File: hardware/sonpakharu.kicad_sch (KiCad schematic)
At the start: 48 parts, among them IC1 ESP32-S3-WROOM-1U-N4, J1 FTDI, J10 EXT4, J11 EXT5, J12 EXT6, J13 EXT7, J14 EXT8, J15 BATT, J16 PWR, J2 ADC1, J3 ADC2, J4 ADC3, J5 ADC4, J6 I2C, J7 EXT1, J8 EXT2, J9 EXT3, Q1 DMG2301L, Q2 S8050, Q3 S8050, SW1 Reset, SW2 Reset, U1 AP2112K-3.3TRG1, U2 MCP73831-2-OT, U3 ADS1115IDGSR

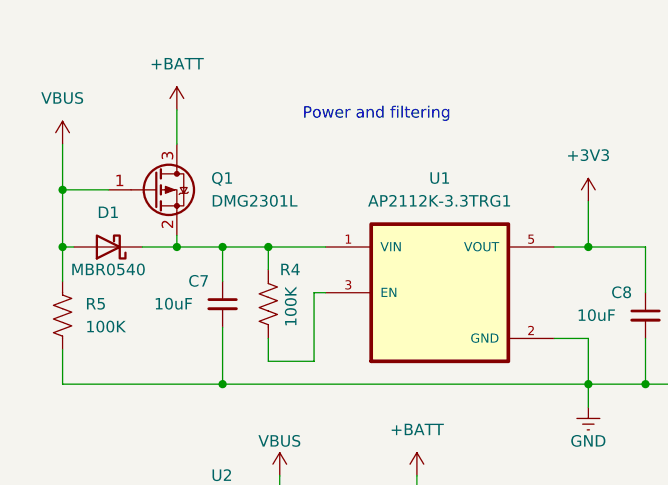
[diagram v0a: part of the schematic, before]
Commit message: added main components mpn
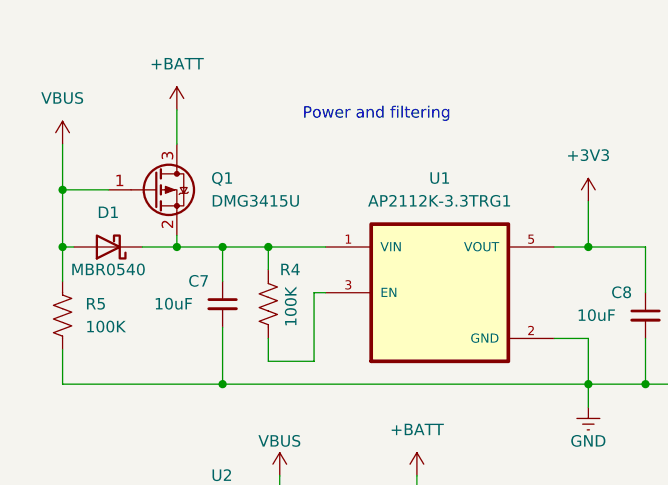
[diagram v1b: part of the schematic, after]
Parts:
- Q1: value DMG2301L -> DMG3415U; MPN (none) -> C96616
- U1: MPN (none) -> C51118
- U2: MPN (none) -> C424093
- U3: MPN (none) -> C37593
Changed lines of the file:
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@@
+      (effects (font (size 1.27 1.27)) hide)
+    )
+    (property "MPN" "C424093" (at 43.18 80.01 0)
       (effects (font (size 1.27 1.27)) hide)
     )
@@
       (effects (font (size 1.27 1.27)) (justify bottom) hide)
     )
+    (property "MPN" "C51118" (at 60.96 48.26 0)
+      (effects (font (size 1.27 1.27)) hide)
+    )
     (pin "1")
     (pin "2")
@@
       (effects (font (size 1.27 1.27)) (justify left))
     )
-    (property "Value" "DMG2301L" (at 35.56 38.1 0)
+    (property "Value" "DMG3415U" (at 35.56 38.1 0)
       (effects (font (size 1.27 1.27)) (justify left))
     )
@@
       (effects (font (size 1.27 1.27)) (justify left) hide)
     )
+    (property "MPN" "C96616" (at 29.21 36.83 0)
+      (effects (font (size 1.27 1.27)) hide)
+    )
     (pin "1")
     (pin "2")
@@
       (effects (font (size 1.27 1.27)) (justify bottom) hide)
     )
-    (pin "1")
+    (property "MPN" "C37593" (at 137.16 172.72 0)
+      (effects (font (size 1.27 1.27)) hide)
+    )
+    (pin "1")

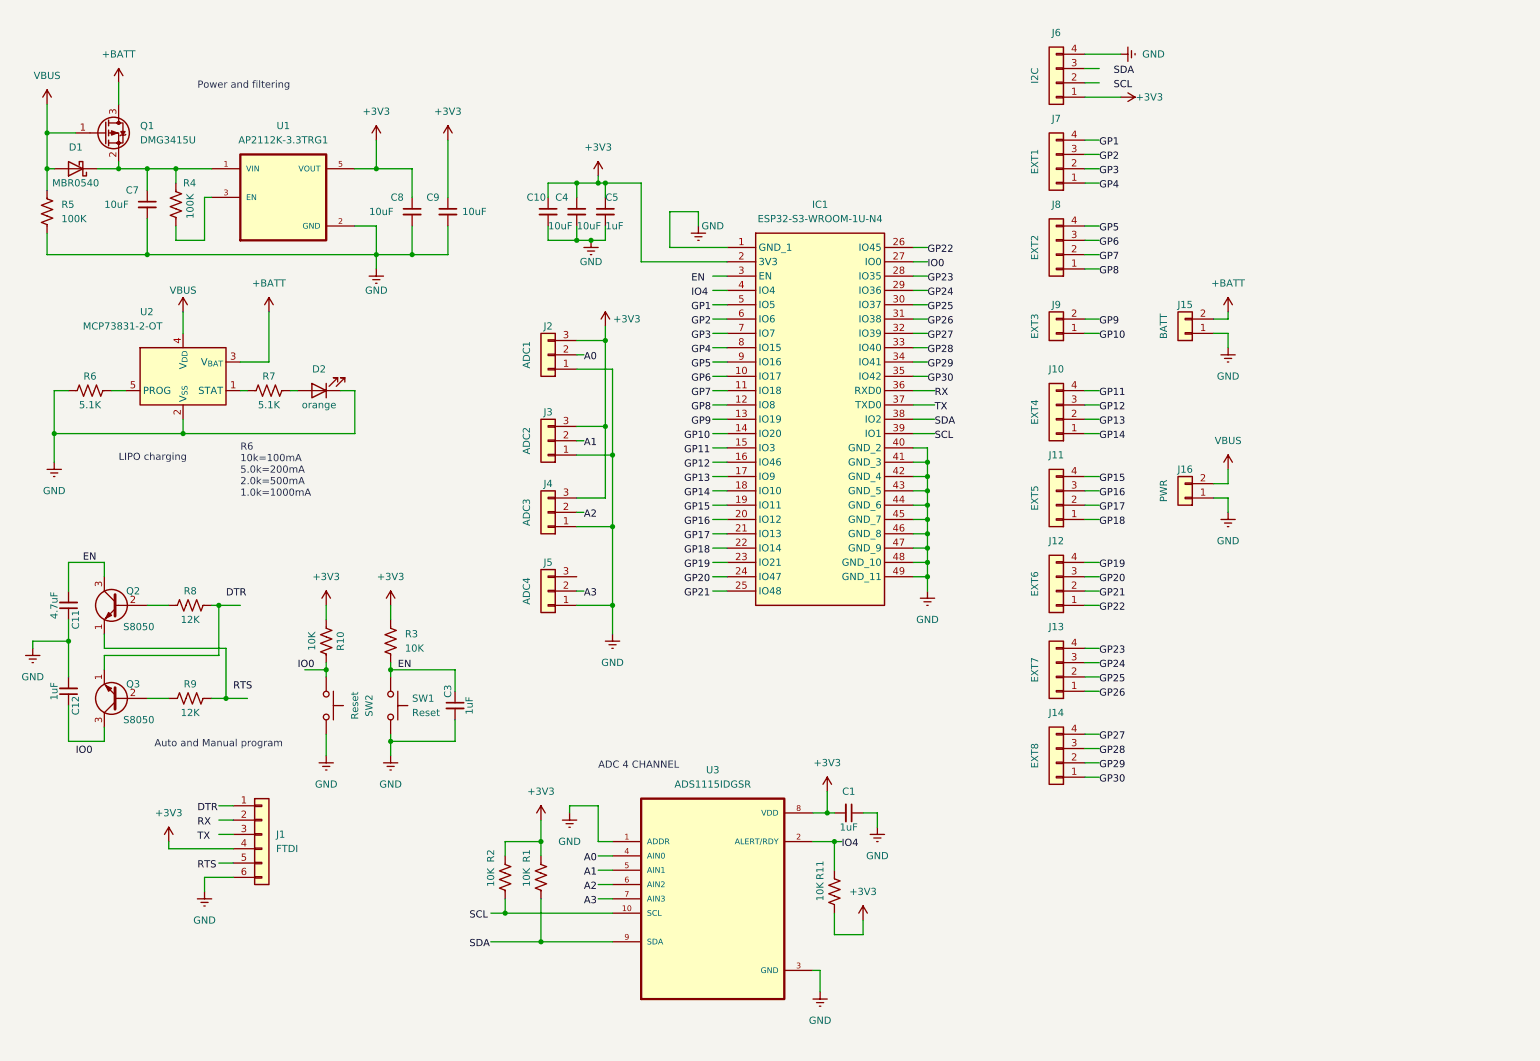
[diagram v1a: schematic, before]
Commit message: Fix: routing
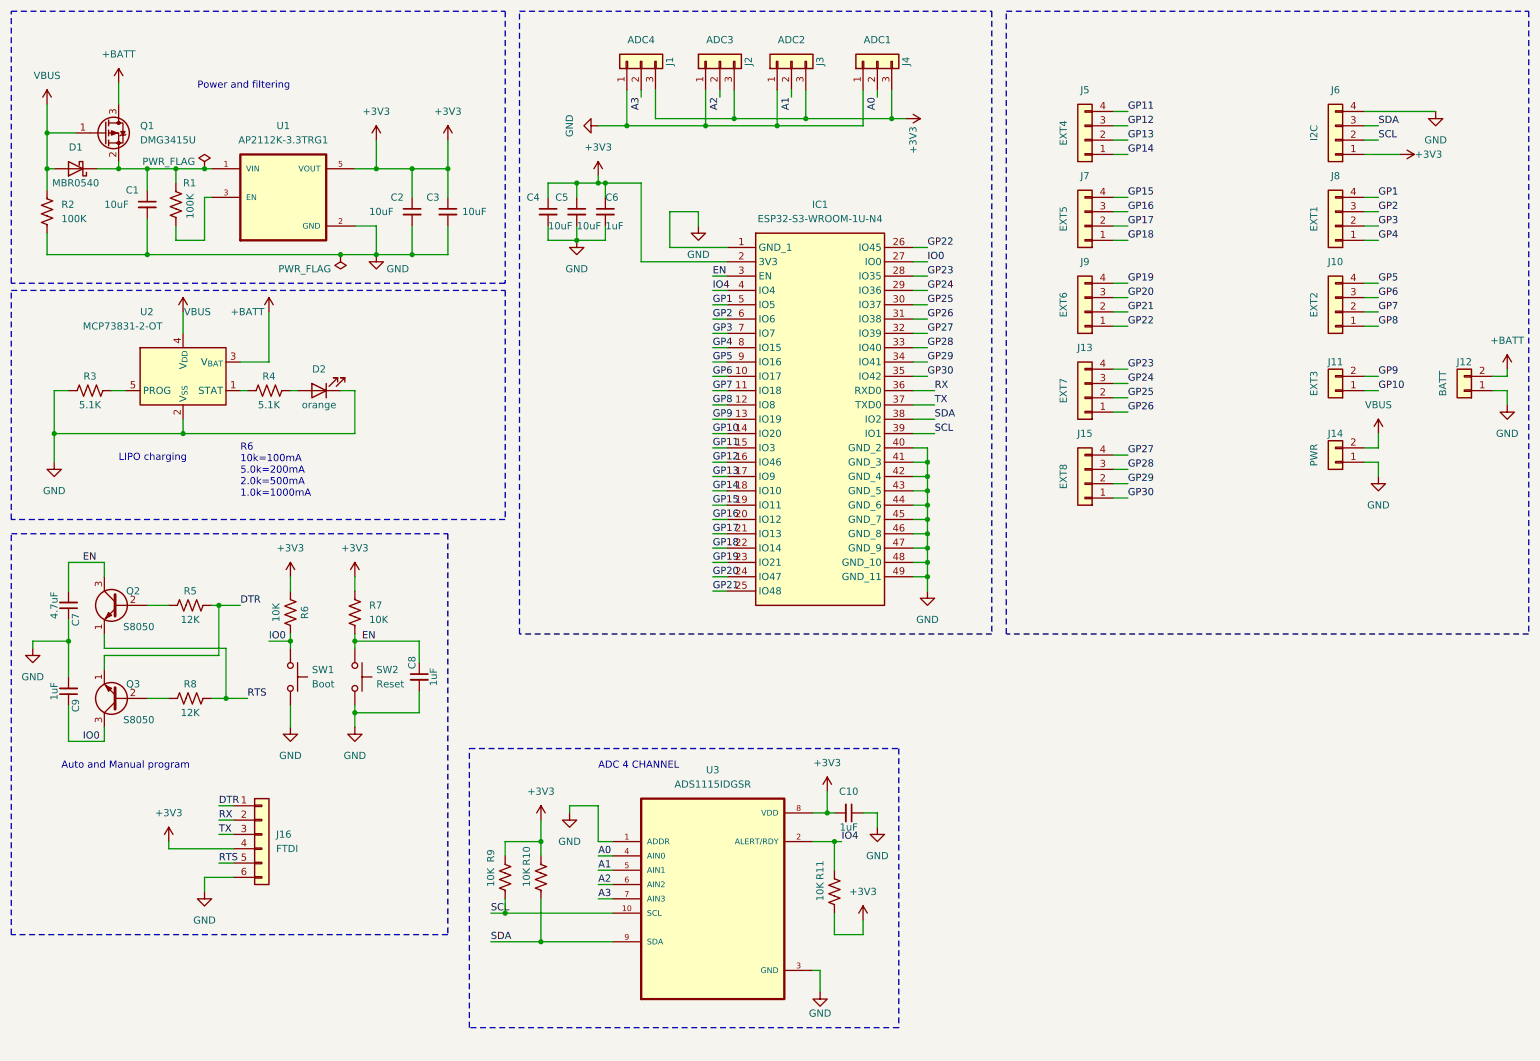
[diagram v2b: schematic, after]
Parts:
- C1: renamed from C7; footprint (none) -> Capacitor_SMD:C_0603_1608Metric; MPN (none) -> C5137578
- C10: renamed from C1; footprint (none) -> Capacitor_SMD:C_0603_1608Metric; MPN (none) -> C363560
- C2: renamed from C8; footprint (none) -> Capacitor_SMD:C_0603_1608Metric; MPN (none) -> C5137578
- C3: renamed from C9; footprint (none) -> Capacitor_SMD:C_0603_1608Metric; MPN (none) -> C5137578
- C4: renamed from C10; footprint (none) -> Capacitor_SMD:C_0603_1608Metric; MPN (none) -> C5137578
- C5: renamed from C4; footprint (none) -> Capacitor_SMD:C_0603_1608Metric; MPN (none) -> C5137578
- C6: renamed from C5; footprint (none) -> Capacitor_SMD:C_0603_1608Metric; MPN (none) -> C363560
- C7: renamed from C11; footprint (none) -> Capacitor_SMD:C_0603_1608Metric; MPN (none) -> C5252398
- C8: renamed from C3; footprint (none) -> Capacitor_SMD:C_0603_1608Metric; MPN (none) -> C363560
- C9: renamed from C12; footprint (none) -> Capacitor_SMD:C_0603_1608Metric; MPN (none) -> C363560
- D1: MPN (none) -> C116159
- D2: footprint (none) -> LED_SMD:LED_0603_1608Metric; MPN (none) -> C779453
- IC1: footprint KiCad:ESP32S3WROOM1UN4 -> RF_Module:ESP32S3WROOM1UN4
- J1: renamed from J5; footprint (none) -> Connector_Molex:Molex_KK-254_AE-6410-03A_1x03_P2.54mm_Vertical
- J10: renamed from J8; footprint (none) -> Connector_Molex:Molex_KK-254_AE-6410-04A_1x04_P2.54mm_Vertical
- J11: renamed from J9; footprint (none) -> Connector_Molex:Molex_KK-254_AE-6410-02A_1x02_P2.54mm_Vertical
- J12: renamed from J15; footprint (none) -> Connector_Molex:Molex_KK-254_AE-6410-02A_1x02_P2.54mm_Vertical
- J13, J6: footprint (none) -> Connector_Molex:Molex_KK-254_AE-6410-04A_1x04_P2.54mm_Vertical
- J14: renamed from J16; footprint (none) -> Connector_Molex:Molex_KK-254_AE-6410-02A_1x02_P2.54mm_Vertical
- J15: renamed from J14; footprint (none) -> Connector_Molex:Molex_KK-254_AE-6410-04A_1x04_P2.54mm_Vertical
- J16: renamed from J1; footprint (none) -> Connector_Molex:Molex_KK-254_AE-6410-06A_1x06_P2.54mm_Vertical
- J2: renamed from J4; footprint (none) -> Connector_Molex:Molex_KK-254_AE-6410-03A_1x03_P2.54mm_Vertical
- J3: footprint (none) -> Connector_Molex:Molex_KK-254_AE-6410-03A_1x03_P2.54mm_Vertical
- J4: renamed from J2; footprint (none) -> Connector_Molex:Molex_KK-254_AE-6410-03A_1x03_P2.54mm_Vertical
- J5: renamed from J10; footprint (none) -> Connector_Molex:Molex_KK-254_AE-6410-04A_1x04_P2.54mm_Vertical
- J7: renamed from J11; footprint (none) -> Connector_Molex:Molex_KK-254_AE-6410-04A_1x04_P2.54mm_Vertical
- J8: renamed from J7; footprint (none) -> Connector_Molex:Molex_KK-254_AE-6410-04A_1x04_P2.54mm_Vertical
- J9: renamed from J12; footprint (none) -> Connector_Molex:Molex_KK-254_AE-6410-04A_1x04_P2.54mm_Vertical
- Q2: footprint Package_TO_SOT_THT:TO-92_Inline -> Package_TO_SOT_SMD:SOT-23; MPN (none) -> C5249674; package (none) -> SOT-23
- Q3: footprint Package_TO_SOT_THT:TO-92_Inline -> Package_TO_SOT_SMD:SOT-23; MPN (none) -> C5249674
- R1: renamed from R4; footprint (none) -> Resistor_SMD:R_0603_1608Metric; MPN (none) -> C25803
- R10: renamed from R1; footprint (none) -> Resistor_SMD:R_0603_1608Metric; MPN (none) -> C25804
- R11: footprint (none) -> Resistor_SMD:R_0603_1608Metric; MPN (none) -> C25804
- R2: renamed from R5; footprint (none) -> Resistor_SMD:R_0603_1608Metric; MPN (none) -> C25803
- R3: renamed from R6; footprint (none) -> Resistor_SMD:R_0603_1608Metric; MPN (none) -> C23186
- R4: renamed from R7; footprint (none) -> Resistor_SMD:R_0603_1608Metric; MPN (none) -> C23186
- R5: renamed from R8; footprint (none) -> Resistor_SMD:R_0603_1608Metric; MPN (none) -> C22790
- R6: renamed from R10; footprint (none) -> Resistor_SMD:R_0603_1608Metric; MPN (none) -> C25804
- R7: renamed from R3; footprint (none) -> Resistor_SMD:R_0603_1608Metric; MPN (none) -> C25804
- R8: renamed from R9; footprint (none) -> Resistor_SMD:R_0603_1608Metric; MPN (none) -> C22790
- R9: renamed from R2; footprint (none) -> Resistor_SMD:R_0603_1608Metric; MPN (none) -> C25804
- SW1: renamed from SW2; value Reset -> Boot; footprint (none) -> Button_Switch_THT:SW_Tactile_Straight_KSA0Axx1LFTR; MPN (none) -> C116647
- SW2: renamed from SW1; footprint (none) -> Button_Switch_THT:SW_Tactile_Straight_KSA0Axx1LFTR; MPN (none) -> C116647
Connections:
- net +3V3: now also J1.3 (Pin_3)
- net A0: now also J4.2 (Pin_2), U3.4 (AIN0)
- net A1: now also J3.2 (Pin_2), U3.5 (AIN1)
- net A2: now also J2.2 (Pin_2), U3.6 (AIN2)
- net A3: now also J1.2 (Pin_2), U3.7 (AIN3)
- net DTR: now also J16.1 (Pin_1), Q3.1 (E), R5.2
- net EN: now also IC1.3 (EN)
- net GP1: now also IC1.5 (IO5), J8.4 (Pin_4)
- net GP10: now also IC1.14 (IO20), J11.1 (Pin_1)
- net GP11: now also IC1.15 (IO3), J5.4 (Pin_4)
- net GP12: now also IC1.16 (IO46), J5.3 (Pin_3)
- net GP13: now also IC1.17 (IO9), J5.2 (Pin_2)
- net GP14: now also IC1.18 (IO10), J5.1 (Pin_1)
- net GP15: now also IC1.19 (IO11), J7.4 (Pin_4)
- net GP16: now also IC1.20 (IO12), J7.3 (Pin_3)
- net GP17: now also IC1.21 (IO13), J7.2 (Pin_2)
- net GP18: now also IC1.22 (IO14), J7.1 (Pin_1)
- net GP19: now also IC1.23 (IO21), J9.4 (Pin_4)
- net GP2: now also IC1.6 (IO6), J8.3 (Pin_3)
- net GP20: now also IC1.24 (IO47), J9.3 (Pin_3)
- net GP21: now also IC1.25 (IO48), J9.2 (Pin_2)
- net GP22: now also IC1.26 (IO45), J9.1 (Pin_1)
- net GP23: now also IC1.28 (IO35), J13.4 (Pin_4)
- net GP24: now also IC1.29 (IO36), J13.3 (Pin_3)
- net GP25: now also IC1.30 (IO37), J13.2 (Pin_2)
- net GP26: now also IC1.31 (IO38), J13.1 (Pin_1)
- net GP27: now also IC1.32 (IO39), J15.4 (Pin_4)
- net GP28: now also IC1.33 (IO40), J15.3 (Pin_3)
- net GP29: now also IC1.34 (IO41), J15.2 (Pin_2)
- net GP3: now also IC1.7 (IO7), J8.2 (Pin_2)
- net GP30: now also IC1.35 (IO42), J15.1 (Pin_1)
- net GP4: now also IC1.8 (IO15), J8.1 (Pin_1)
- net GP5: now also IC1.9 (IO16), J10.4 (Pin_4)
- net GP6: now also IC1.10 (IO17), J10.3 (Pin_3)
- net GP7: now also IC1.11 (IO18), J10.2 (Pin_2)
- net GP8: now also IC1.12 (IO8), J10.1 (Pin_1)
- net GP9: now also IC1.13 (IO19), J11.2 (Pin_2)
- net IO0: now also C9.1, IC1.27 (IO0), Q3.3 (C), R6.2, SW1.1
- net IO4: now also IC1.4 (IO4), R11.1, U3.2 (ALERT/RDY)
- net RTS: now also J16.5 (Pin_5), Q2.1 (E), R8.2
- net RX: now also IC1.36 (RXD0), J16.2 (Pin_2)
- net SCL: now also IC1.39 (IO1), J6.2 (Pin_2), R9.2, U3.10 (SCL)
- net SDA: now also IC1.38 (IO2), J6.3 (Pin_3), R10.2, U3.9 (SDA)
- net TX: now also IC1.37 (TXD0), J16.3 (Pin_3)
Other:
- company: (none) -> Rajendra Khope
- title: Khope ka Kida -> Sonpakharu
- moved on the sheet: C8, J1, J10, J11, J12, J13, J14, J15, J2, J3, J4, J5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

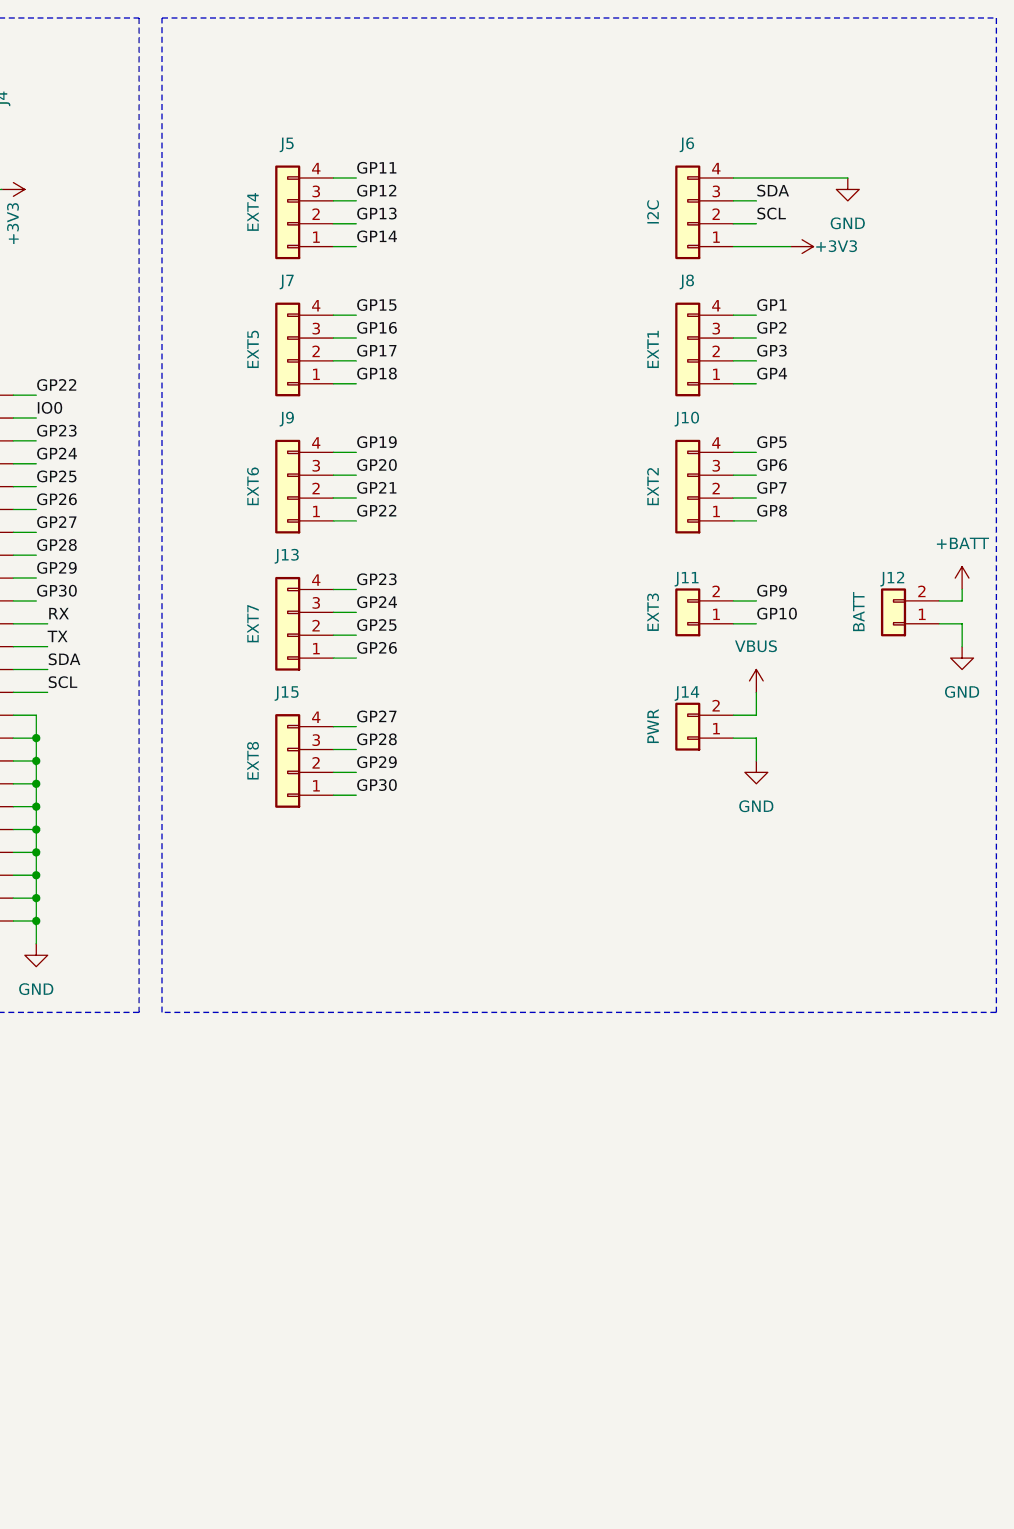
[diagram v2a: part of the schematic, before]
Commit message: added 485
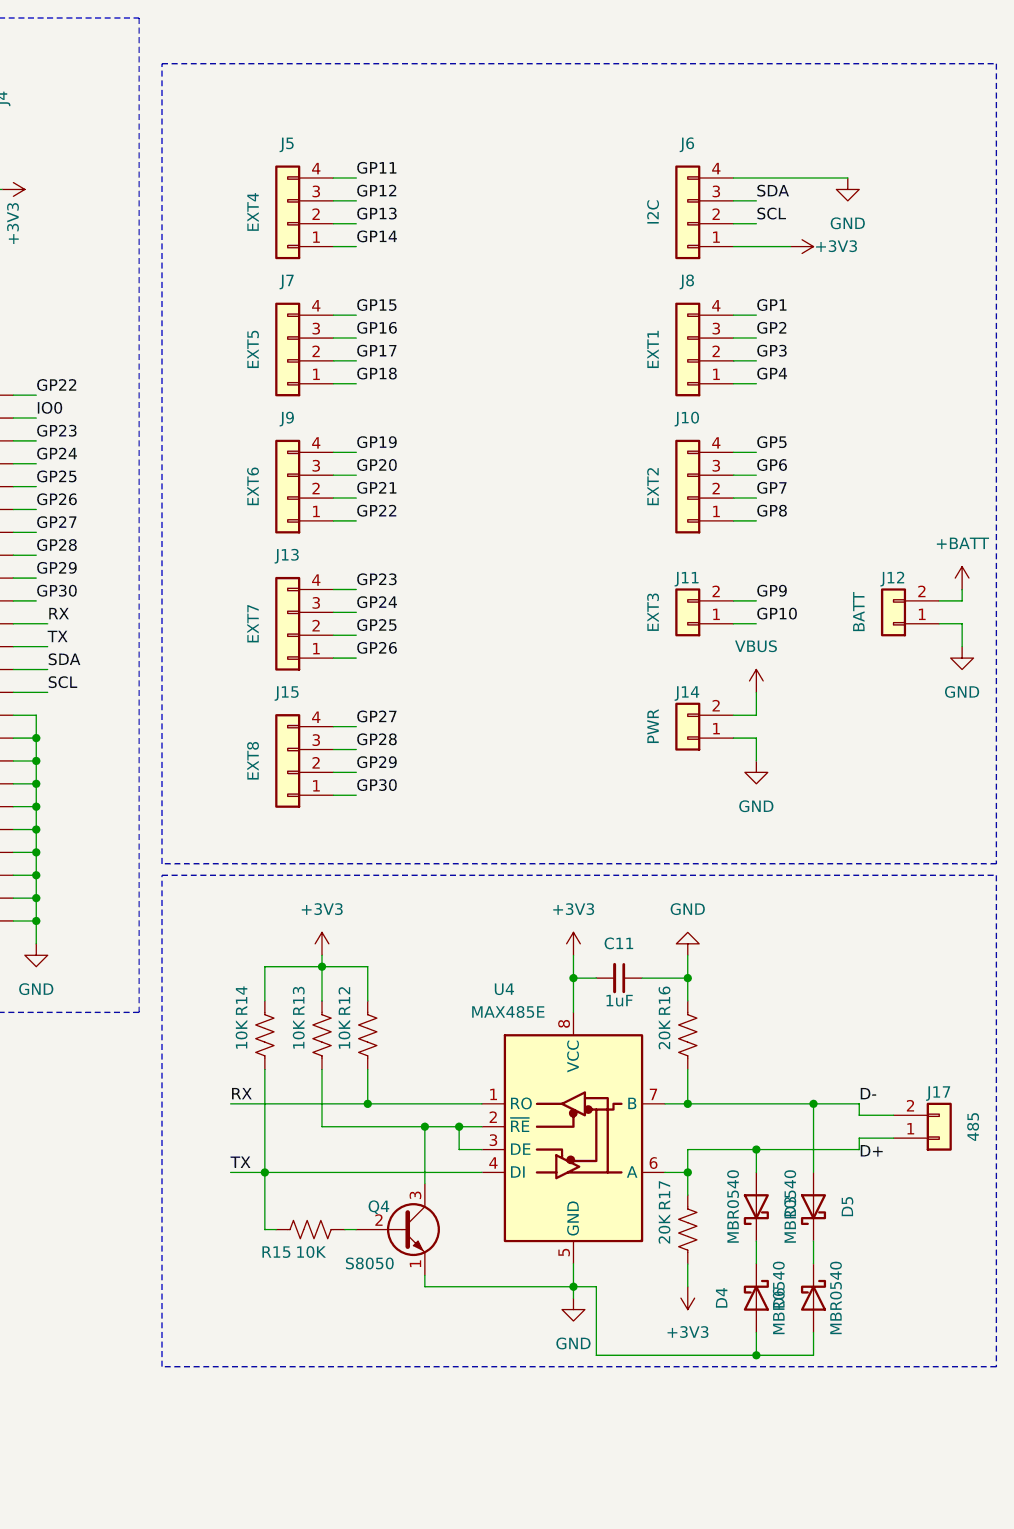
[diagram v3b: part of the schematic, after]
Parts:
- added C11: 1uF, Capacitor_SMD:C_0603_1608Metric, symbol Device:C_Small
- added D3, D4, D5, D6: MBR0540, Diode_SMD:D_SOD-123, symbol Diode:MBR0540
- added J17: 485, Connector_Molex:Molex_KK-254_AE-6410-02A_1x02_P2.54mm_Vertical, symbol Connector_Generic:Conn_01x02
- added Q4: S8050, Package_TO_SOT_SMD:SOT-23, symbol Transistor_BJT:S8050
- added R12, R13, R14, R15: 10K, Resistor_SMD:R_0603_1608Metric, symbol Device:R_US
- added R16, R17: 20K, Resistor_SMD:R_0603_1608Metric, symbol Device:R_US
- added U4: MAX485E, MAX485SOIC8:21-0041B_8_MXM, symbol Interface_UART:MAX485E
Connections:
- net +3V3: now also C11.2, R12.1, R13.1, R14.1, R17.2, U4.8 (VCC)
- net GND: now also C11.1, D4.2 (A), D6.2 (A), Q4.1 (E), R16.1, U4.5 (GND)
- net RX: now also R12.2, U4.1 (RO)
- net TX: now also R14.2, R15.1, U4.4 (DI)
- new net: Q4.2 (B), R15.2
- new net: Q4.3 (C), R13.2, U4.2 (~{RE}), U4.3 (DE)
- new net: D3.1 (K), D4.1 (K)
- new net: D3.2 (A), J17.1 (Pin_1), R17.1, U4.6 (A)
- new net: D5.1 (K), D6.1 (K)
- new net D-: D5.2 (A), J17.2 (Pin_2), R16.2, U4.7 (B)
